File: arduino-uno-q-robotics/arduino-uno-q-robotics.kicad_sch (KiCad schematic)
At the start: 9 parts, among them J1 Conn_02x30_Odd_Even, J2 Conn_02x30_Odd_Even, J3 Connector_FFC-FPC, J4 Connector_FFC-FPC, U1 LSM6DSO32, U2 TCA9803

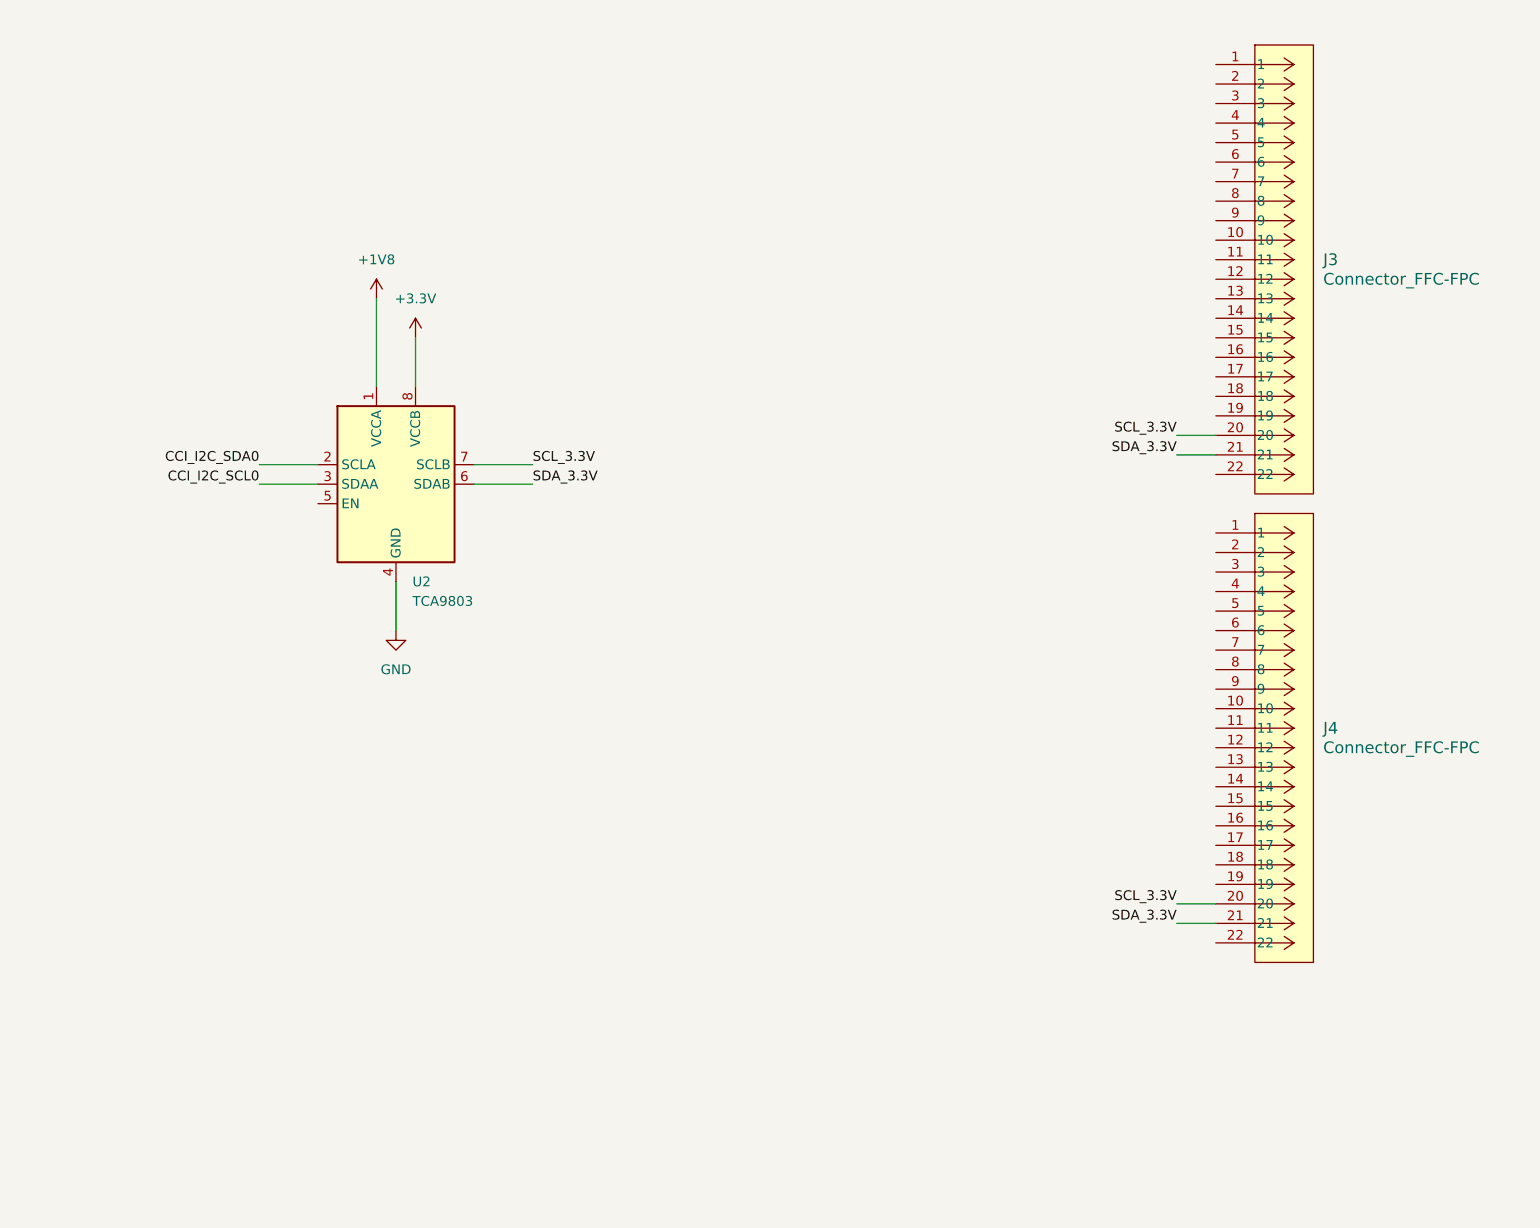
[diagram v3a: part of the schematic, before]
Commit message: Connect camera data lines to camera connector
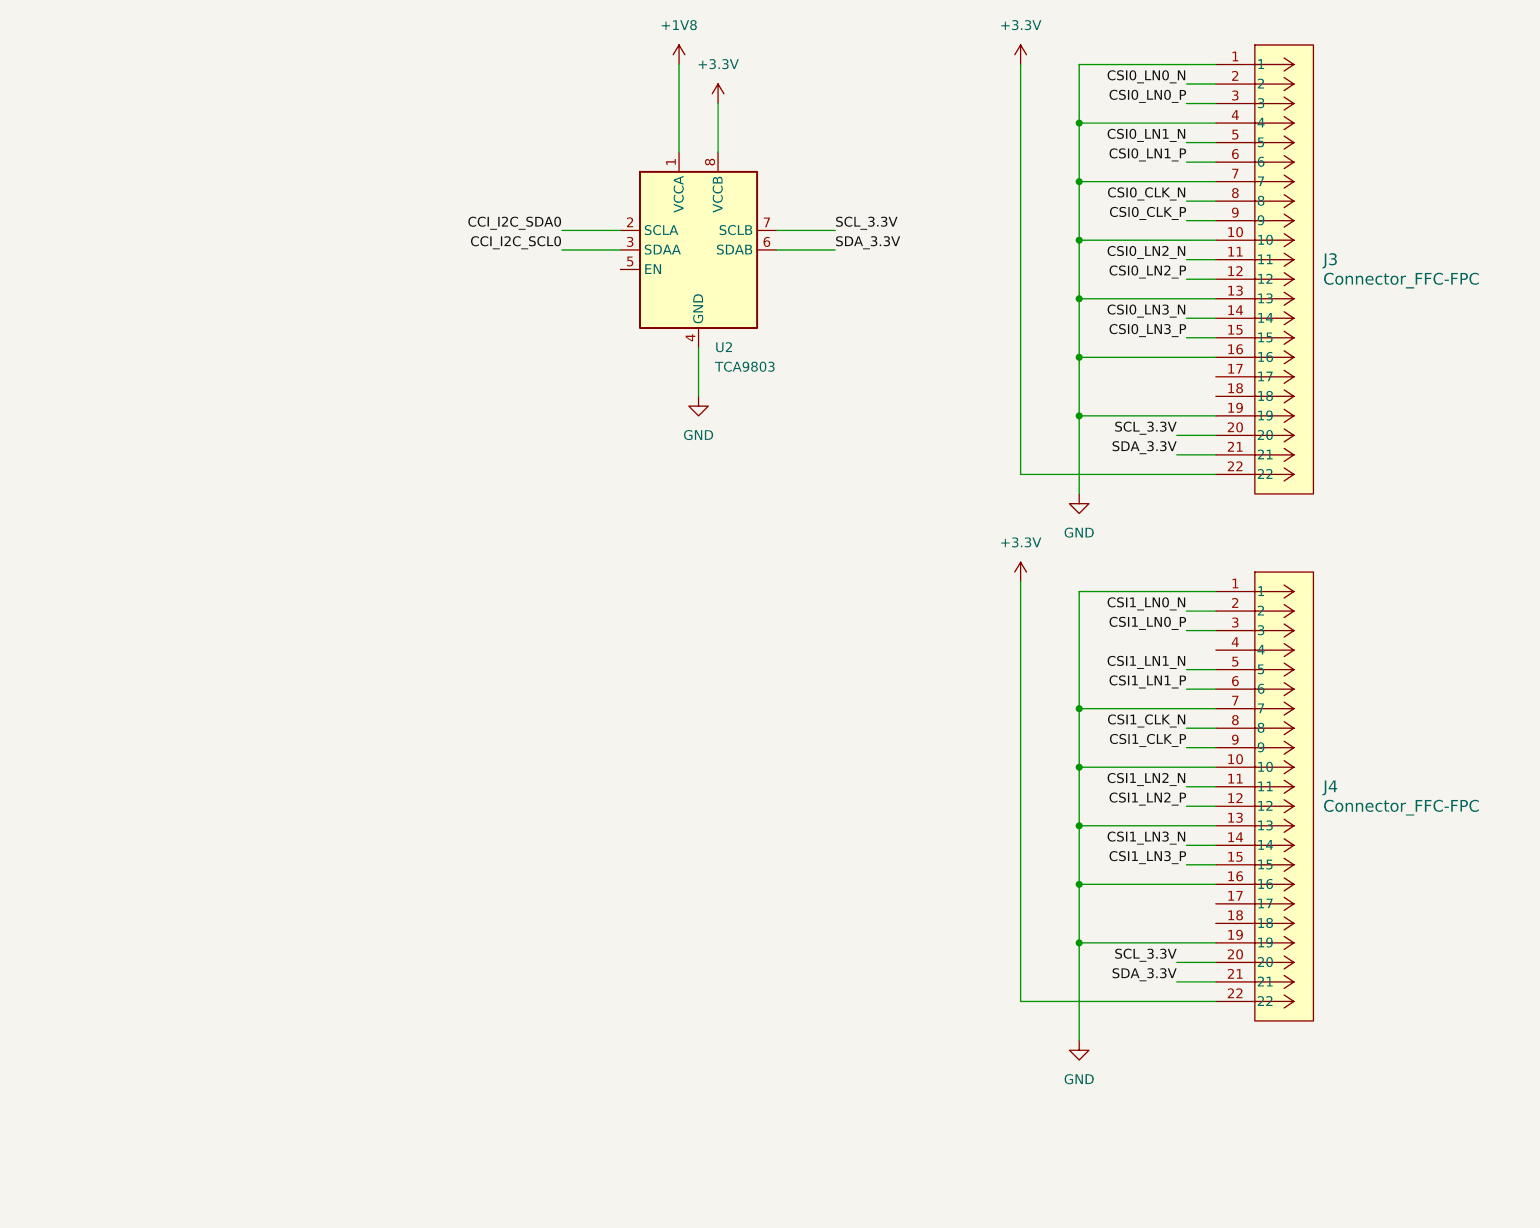
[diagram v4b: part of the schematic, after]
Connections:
- net +3.3V: now also J3.22, J4.22
- net CSI0_CLK_N: now also J3.8
- net CSI0_CLK_P: now also J3.9
- net CSI0_LN0_N: now also J3.2
- net CSI0_LN0_P: now also J3.3
- net CSI0_LN1_N: now also J3.5
- net CSI0_LN1_P: now also J3.6
- net CSI0_LN2_N: now also J3.11
- net CSI0_LN2_P: now also J3.12
- net CSI0_LN3_N: now also J3.14
- net CSI0_LN3_P: now also J3.15
- net CSI1_CLK_N: now also J4.8
- net CSI1_CLK_P: now also J4.9
- net CSI1_LN0_N: now also J4.2
- net CSI1_LN0_P: now also J4.3
- net CSI1_LN1_N: now also J4.5
- net CSI1_LN1_P: now also J4.6
- net CSI1_LN2_N: now also J4.11
- net CSI1_LN2_P: now also J4.12
- net CSI1_LN3_N: now also J4.14
- net CSI1_LN3_P: now also J4.15
- net GND: now also J3.1, J3.10, J3.13, J3.16, J3.19, J3.4, J3.7, J4.1, J4.10, J4.13, J4.16, J4.19, J4.7
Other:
- moved on the sheet: J4, U2

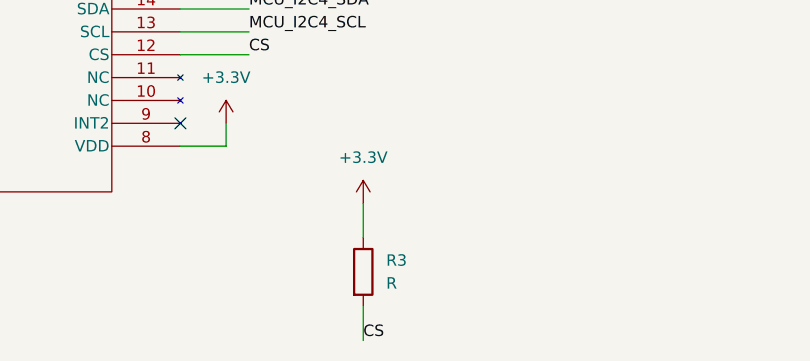
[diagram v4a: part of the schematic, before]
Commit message: Add resistor footprint
Resistor_SMD:R_0603_1608Metric_Pad0.98x0.95mm
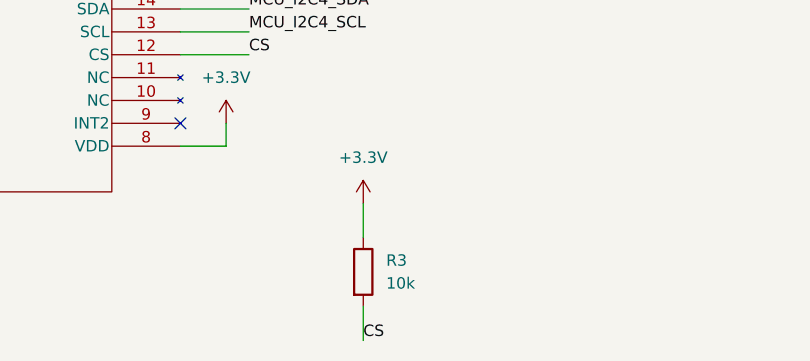
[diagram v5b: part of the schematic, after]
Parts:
- R1, R2: footprint (none) -> Resistor_SMD:R_0603_1608Metric_Pad0.98x0.95mm_HandSolder
- R3: value R -> 10k; footprint (none) -> Resistor_SMD:R_0603_1608Metric_Pad0.98x0.95mm_HandSolder
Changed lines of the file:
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@@
 			)
 		)
-		(property "Footprint" ""
+		(property "Footprint" "Resistor_SMD:R_0603_1608Metric_Pad0.98x0.95mm_HandSolder"
 			(at 35.052 140.97 90)
 			(effects
@@
 			)
 		)
-		(property "Footprint" ""
+		(property "Footprint" "Resistor_SMD:R_0603_1608Metric_Pad0.98x0.95mm_HandSolder"
 			(at 17.272 140.97 90)
 			(effects
@@
 			)
 		)
-		(property "Value" "R"
+		(property "Value" "10k"
 			(at 100.33 275.5899 0)
 			(effects
@@
 			)
 		)
-		(property "Footprint" ""
+		(property "Footprint" "Resistor_SMD:R_0603_1608Metric_Pad0.98x0.95mm_HandSolder"
 			(at 96.012 274.32 90)
 			(effects

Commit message: Change FPC footprint and 3D model
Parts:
- J3, J4: footprint robotics-footprints:CON_5019512230 -> robotics-footprints:CON_5051102291_MOL
- U1: footprint robotics-footprints:LGA-14L_2P5X3X0P83_STM -> LGA-14L_2P5X3X0P83_STM
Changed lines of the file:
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@@
 			)
 		)
-		(property "Footprint" "robotics-footprints:LGA-14L_2P5X3X0P83_STM"
+		(property "Footprint" "LGA-14L_2P5X3X0P83_STM"
 			(at 56.642 268.224 0)
 			(effects
@@
 			)
 		)
-		(property "Footprint" "robotics-footprints:CON_5019512230"
+		(property "Footprint" "robotics-footprints:CON_5051102291_MOL"
 			(at 381 20.32 0)
 			(effects
@@
 			)
 		)
-		(property "Description" "Power symbol creates a global label with name \"VBAT\""
+		(property "Description" "Power symbol creates a global label with name \"VBUS\""
 			(at 106.68 30.48 0)
 			(effects
@@
 			)
 		)
-		(property "Footprint" "robotics-footprints:CON_5019512230"
+		(property "Footprint" "robotics-footprints:CON_5051102291_MOL"
 			(at 381 88.9 0)
 			(effects

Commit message: Switch JMEDIA header to THT version
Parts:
- J2: footprint Connector_PinHeader_1.27mm:PinHeader_2x30_P1.27mm_Vertical_SMD -> Connector_PinHeader_1.27mm:PinHeader_2x30_P1.27mm_Vertical
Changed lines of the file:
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@@
 			)
 		)
-		(property "Footprint" "Connector_PinHeader_1.27mm:PinHeader_2x30_P1.27mm_Vertical_SMD"
+		(property "Footprint" "Connector_PinHeader_1.27mm:PinHeader_2x30_P1.27mm_Vertical"
 			(at 157.48 67.31 0)
 			(effects
